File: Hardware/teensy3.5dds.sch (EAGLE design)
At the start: 105 parts, among them IC1 AD8034, IC2 AD8034, IC3 AD8034, IC4 AD8034, IC5 AD8034, IC6 AD737KRZ-R7, IC7 AD8034, IC8 AD8034, J1 1776275-2, J2 1776275-2, Q1 10MHz, U1 TEENSY_3.5/3.6_BASIC, U2 ATMEGA32U4-AU, X1 1-227161-0

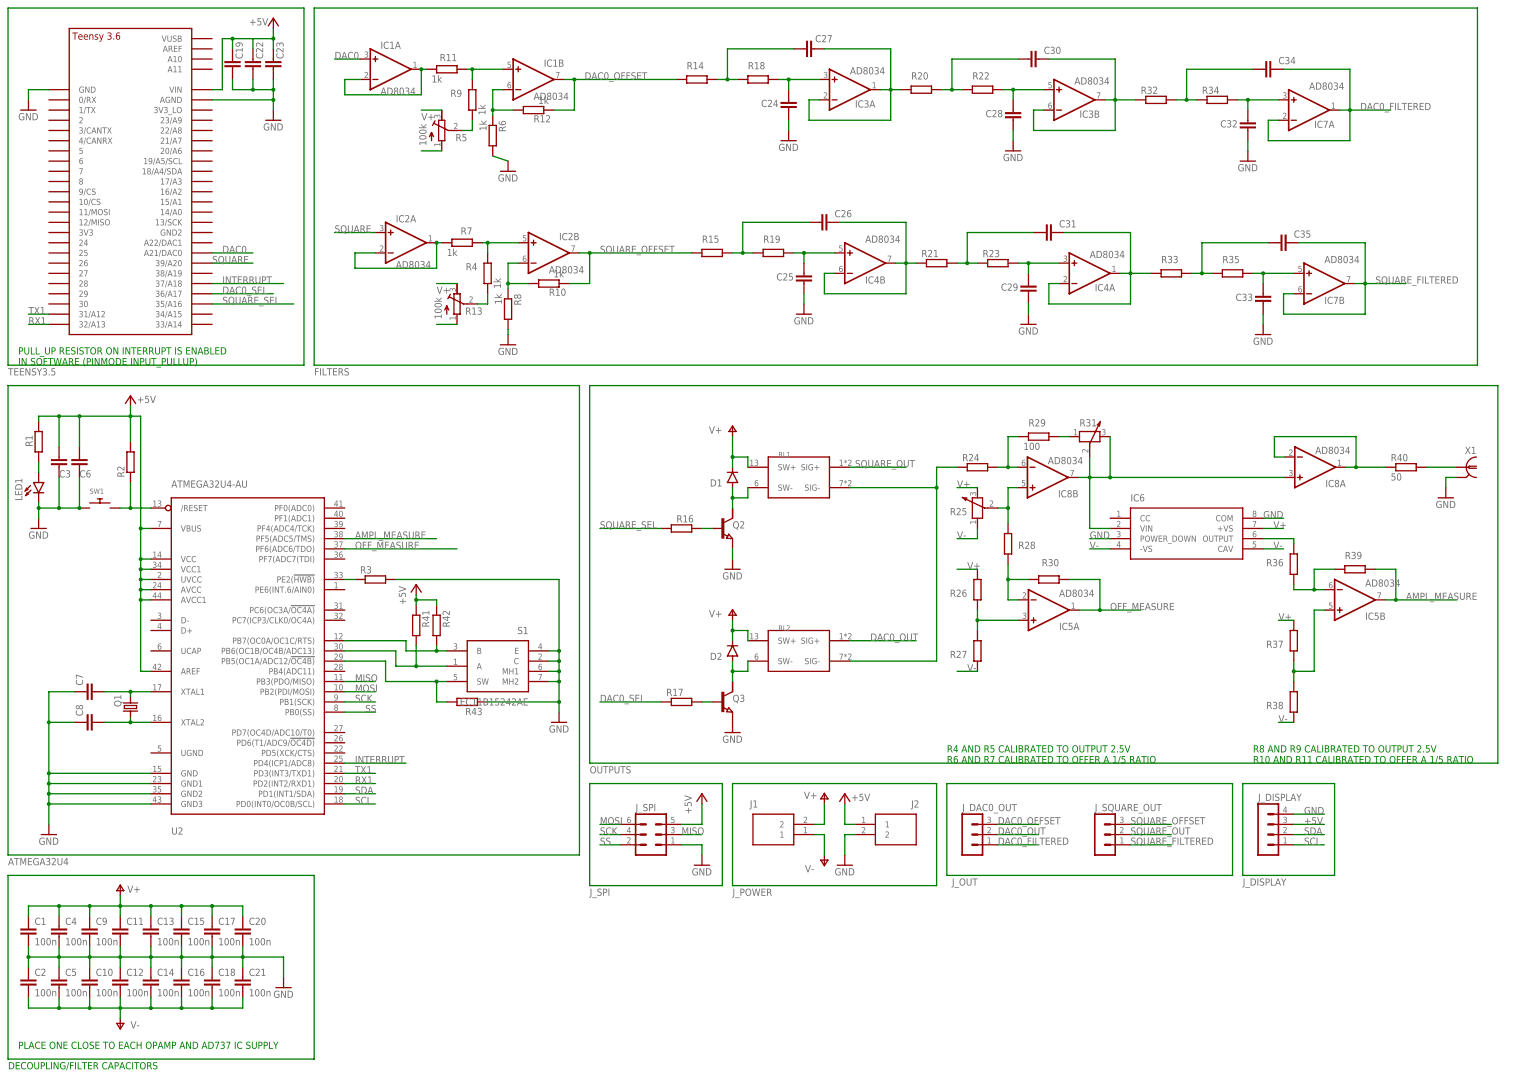
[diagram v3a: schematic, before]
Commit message: an actually working filter for the square wave
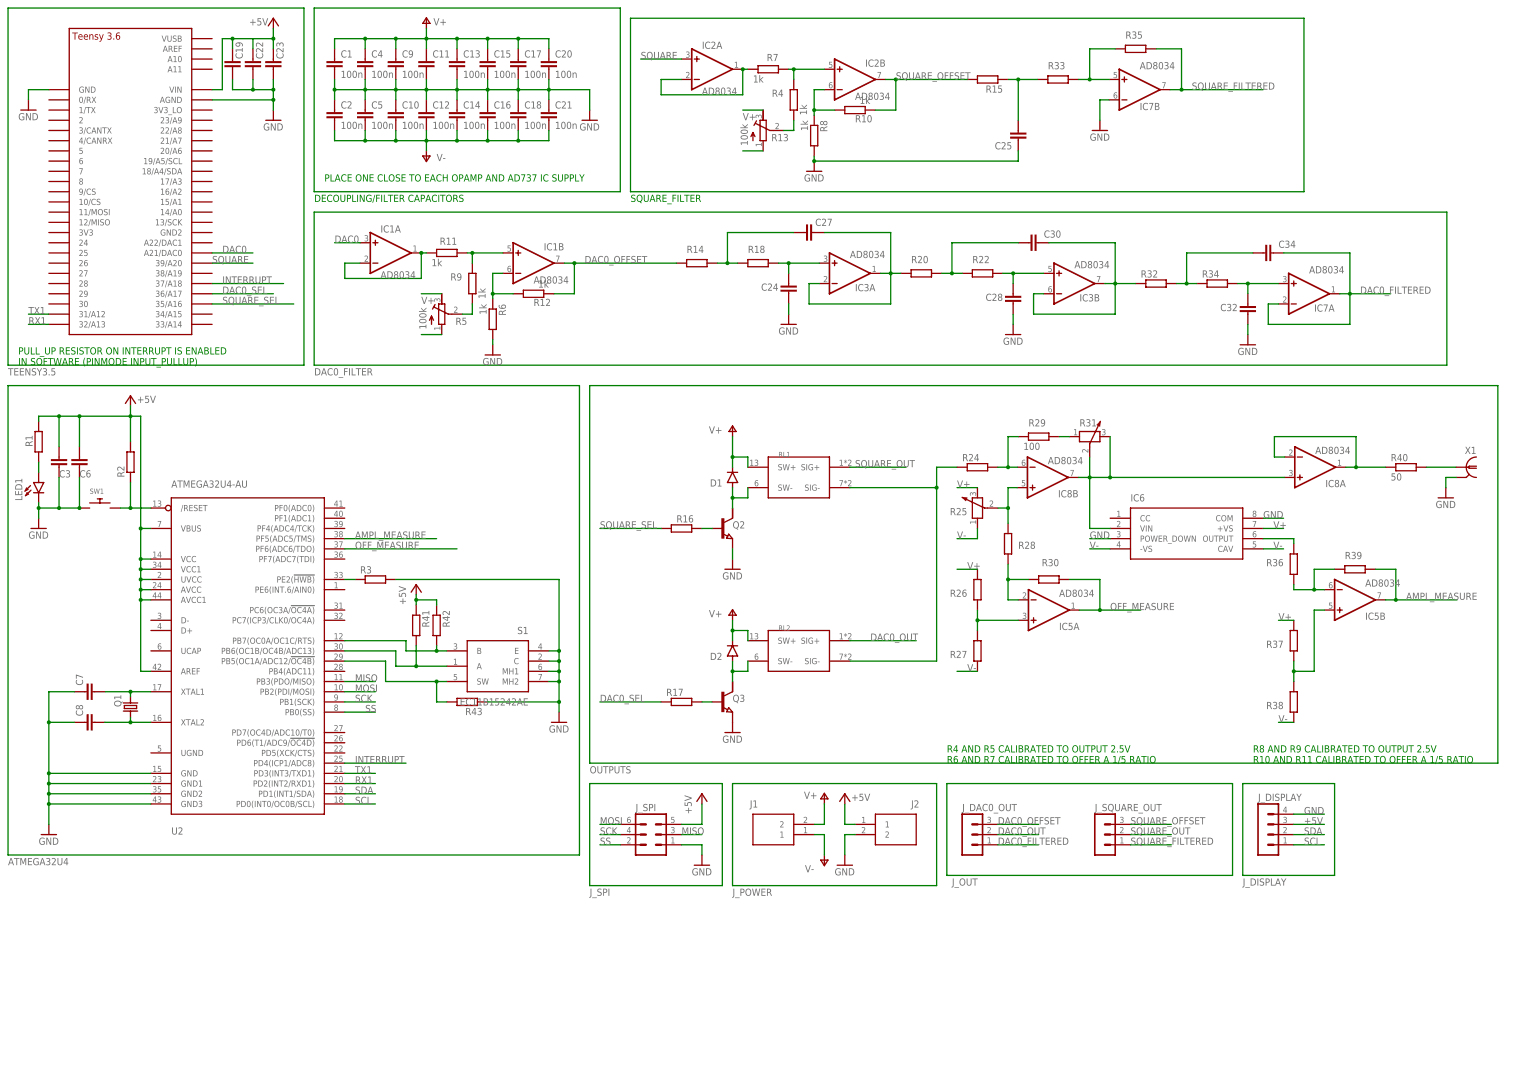
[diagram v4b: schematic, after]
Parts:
- removed C26, C31, C35: 100p, rcl:C-EUC0805
- removed C29, C33: 10p, rcl:C-EUC0805
- removed IC4: AD8034, linear:TL082D
- removed R19: 4.75k, rcl:R-EU_M0805
- removed R21: 150, rcl:R-EU_R0805
- removed R23: 3.74k, rcl:R-EU_R0805
- C25: value 10p -> (none)
- R15: value 130 -> (none); device rcl:R-EU_M0805 -> rcl:R-EU_R0805
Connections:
- removed net N$66: C31.2, R21.2, R23.1
- removed net N$67: C31.1, IC4A.-IN, IC4A.OUT, R33.1
- removed net N$68: C29.2, IC4A.+IN, R23.2
- removed net N$69: C26.1, R15.2, R19.1
- removed net N$70: C26.2, IC4B.-IN, IC4B.OUT, R21.1
- removed net N$71: C25.2, IC4B.+IN, R19.2
- removed net N$76: C35.1, R33.2, R35.1
- removed net N$78: C33.2, IC7B.+IN, R35.2
- new net N$1: IC7B.+IN, R33.2, R35.1
- new net N$34: C25.2, R15.1, R33.1
- net GND: now also IC7B.-IN; no longer C29.1, C33.1
- net SQUARE_FILTERED: now also R35.2; no longer C35.2, IC7B.-IN
- net SQUARE_OFFSET: now also R15.2; no longer R15.1
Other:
- note added: "SQUARE_FILTER"
- moved on the sheet: C1, C10, C11, C12, C13, C14, C15, C16, C17, C18, C2, C20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

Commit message: board redisegn
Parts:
- removed C11: (no value), rcl:C-EUC0805
- removed C12: 100n, rcl:C-EUC0805
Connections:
- net GND: no longer C11.2, C12.1
- net N$25: now also U2.PC7(ICP3/CLK0/OC4A); no longer U2.PB6(OC1B/OC4B/ADC13)
- net N$29: now also U2.PB6(OC1B/OC4B/ADC13); no longer U2.PB5(OC1A/ADC12/!OC4B)
- net N$8: now also U2.PC6(OC3A/!OC4A); no longer U2.PB7(OC0A/OC1C/RTS)
- net V+: no longer C11.1
- net V-: no longer C12.2
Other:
- moved on the sheet: C25
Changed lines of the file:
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@@
 <setting verticaltext="up"/>
 </settings>
-<grid distance="0.1" unitdist="inch" unit="inch" style="lines" multiple="1" display="yes" altdistance="0.05" altunitdist="inch" altunit="inch"/>
+<grid distance="0.1" unitdist="inch" unit="inch" style="lines" multiple="1" display="no" altdistance="0.01" altunitdist="inch" altunit="inch"/>
 <layers>
 <layer number="1" name="Top" color="4" fill="1" visible="no" active="no"/>
@@
 <part name="C4" library="rcl" library_urn="urn:adsk.eagle:library:334" deviceset="C-EU" device="C0805" package3d_urn="urn:adsk.eagle:package:23617/2" value="100n"/>
 <part name="C9" library="rcl" library_urn="urn:adsk.eagle:library:334" deviceset="C-EU" device="C0805" package3d_urn="urn:adsk.eagle:package:23617/2" value="100n"/>
-<part name="C11" library="rcl" library_urn="urn:adsk.eagle:library:334" deviceset="C-EU" device="C0805" package3d_urn="urn:adsk.eagle:package:23617/2"/>
 <part name="C13" library="rcl" library_urn="urn:adsk.eagle:library:334" deviceset="C-EU" device="C0805" package3d_urn="urn:adsk.eagle:package:23617/2" value="100n"/>
 <part name="C15" library="rcl" library_urn="urn:adsk.eagle:library:334" deviceset="C-EU" device="C0805" package3d_urn="urn:adsk.eagle:package:23617/2" value="100n"/>
@@
 <part name="C5" library="rcl" library_urn="urn:adsk.eagle:library:334" deviceset="C-EU" device="C0805" package3d_urn="urn:adsk.eagle:package:23617/2" value="100n"/>
 <part name="C10" library="rcl" library_urn="urn:adsk.eagle:library:334" deviceset="C-EU" device="C0805" package3d_urn="urn:adsk.eagle:package:23617/2" value="100n"/>
-<part name="C12" library="rcl" library_urn="urn:adsk.eagle:library:334" deviceset="C-EU" device="C0805" package3d_urn="urn:adsk.eagle:package:23617/2" value="100n"/>
 <part name="C14" library="rcl" library_urn="urn:adsk.eagle:library:334" deviceset="C-EU" device="C0805" package3d_urn="urn:adsk.eagle:package:23617/2" value="100n"/>
 <part name="C16" library="rcl" library_urn="urn:adsk.eagle:library:334" deviceset="C-EU" device="C0805" package3d_urn="urn:adsk.eagle:package:23617/2" value="100n"/>
@@
 <part name="R15" library="rcl" library_urn="urn:adsk.eagle:library:334" deviceset="R-EU_" device="R0805" package3d_urn="urn:adsk.eagle:package:23553/2"/>
 <part name="C25" library="rcl" library_urn="urn:adsk.eagle:library:334" deviceset="C-EU" device="C0805" package3d_urn="urn:adsk.eagle:package:23617/2"/>
+<part name="GND4" library="supply1" library_urn="urn:adsk.eagle:library:371" deviceset="GND" device=""/>
 </parts>
 <sheets>
@@
 <attribute name="VALUE" x="67.564" y="15.621" size="1.778" layer="96"/>
 </instance>
-<instance part="C11" gate="G$1" x="73.66" y="20.32" smashed="yes">
-<attribute name="NAME" x="75.184" y="20.701" size="1.778" layer="95"/>
-<attribute name="VALUE" x="75.184" y="15.621" size="1.778" layer="96"/>
-</instance>
 <instance part="C13" gate="G$1" x="81.28" y="20.32" smashed="yes">
 <attribute name="NAME" x="82.804" y="20.701" size="1.778" layer="95"/>
@@
 <attribute name="VALUE" x="67.564" y="2.921" size="1.778" layer="96"/>
 </instance>
-<instance part="C12" gate="G$1" x="73.66" y="7.62" smashed="yes">
-<attribute name="NAME" x="75.184" y="8.001" size="1.778" layer="95"/>
-<attribute name="VALUE" x="75.184" y="2.921" size="1.778" layer="96"/>
-</instance>
 <instance part="C14" gate="G$1" x="81.28" y="7.62" smashed="yes">
 <attribute name="NAME" x="82.804" y="8.001" size="1.778" layer="95"/>
@@
 <attribute name="VALUE" x="217.17" y="18.542" size="1.778" layer="96" rot="R180"/>
 </instance>
-<instance part="C25" gate="G$1" x="220.98" y="0" smashed="yes" rot="R180">
-<attribute name="NAME" x="219.456" y="-0.381" size="1.778" layer="95" rot="R180"/>
-<attribute name="VALUE" x="219.456" y="4.699" size="1.778" layer="96" rot="R180"/>
+<instance part="C25" gate="G$1" x="220.98" y="2.54" smashed="yes" rot="R180">
+<attribute name="NAME" x="219.456" y="2.159" size="1.778" layer="95" rot="R180"/>
+<attribute name="VALUE" x="219.456" y="7.239" size="1.778" layer="96" rot="R180"/>
+</instance>
+<instance part="GND4" gate="1" x="220.98" y="-7.62" smashed="yes">
+<attribute name="VALUE" x="218.44" y="-10.16" size="1.778" layer="96"/>
 </instance>
 </instances>
@@
 <pinref part="C13" gate="G$1" pin="2"/>
 <wire x1="81.28" y1="12.7" x2="81.28" y2="15.24" width="0.1524" layer="91"/>
-<pinref part="C11" gate="G$1" pin="2"/>
 <wire x1="73.66" y1="15.24" x2="73.66" y2="12.7" width="0.1524" layer="91"/>
 <junction x="73.66" y="12.7"/>
-<pinref part="C12" gate="G$1" pin="1"/>
 <wire x1="73.66" y1="10.16" x2="73.66" y2="12.7" width="0.1524" layer="91"/>
 <pinref part="C9" gate="G$1" pin="2"/>
@@
 </segment>
 <segment>
+<pinref part="R8" gate="G$1" pin="2"/>
 <pinref part="GND17" gate="1" pin="GND"/>
-<pinref part="R8" gate="G$1" pin="2"/>
 <wire x1="170.18" y1="-5.08" x2="170.18" y2="-3.81" width="0.1524" layer="91"/>
-<pinref part="C25" gate="G$1" pin="1"/>
-<wire x1="220.98" y1="-2.54" x2="220.98" y2="-5.08" width="0.1524" layer="91"/>
-<wire x1="220.98" y1="-5.08" x2="170.18" y2="-5.08" width="0.1524" layer="91"/>
-<junction x="170.18" y="-5.08"/>
 </segment>
 <segment>
@@
 <wire x1="241.3" y1="10.16" x2="241.3" y2="5.08" width="0.1524" layer="91"/>
 </segment>
+<segment>
+<pinref part="C25" gate="G$1" pin="1"/>
+<wire x1="220.98" y1="0" x2="220.98" y2="-5.08" width="0.1524" layer="91"/>
+<pinref part="GND4" gate="1" pin="GND"/>
+</segment>
 </net>
 <net name="DAC0" class="1">
@@
 <wire x1="66.04" y1="22.86" x2="66.04" y2="25.4" width="0.1524" layer="91"/>
 <junction x="66.04" y="25.4"/>
-<pinref part="C11" gate="G$1" pin="1"/>
 <wire x1="73.66" y1="22.86" x2="73.66" y2="25.4" width="0.1524" layer="91"/>
 <pinref part="C13" gate="G$1" pin="1"/>
@@
 <wire x1="66.04" y1="2.54" x2="66.04" y2="0" width="0.1524" layer="91"/>
 <junction x="66.04" y="0"/>
-<pinref part="C12" gate="G$1" pin="2"/>
 <wire x1="73.66" y1="2.54" x2="73.66" y2="0" width="0.1524" layer="91"/>
 <pinref part="C14" gate="G$1" pin="2"/>
@@
 <net name="N$8" class="0">
 <segment>
-<pinref part="U2" gate="G$1" pin="PB7(OC0A/OC1C/RTS)"/>
-<wire x1="53.34" y1="-124.46" x2="68.58" y2="-124.46" width="0.1524" layer="91"/>
-<wire x1="68.58" y1="-124.46" x2="68.58" y2="-127" width="0.1524" layer="91"/>
 <pinref part="S1" gate="G$1" pin="B"/>
 <wire x1="68.58" y1="-127" x2="76.2" y2="-127" width="0.1524" layer="91"/>
@@
 <wire x1="76.2" y1="-125.73" x2="76.2" y2="-127" width="0.1524" layer="91"/>
 <junction x="76.2" y="-127"/>
+<pinref part="U2" gate="G$1" pin="PC6(OC3A/!OC4A)"/>
+<wire x1="53.34" y1="-116.84" x2="68.58" y2="-116.84" width="0.1524" layer="91"/>
+<wire x1="68.58" y1="-116.84" x2="68.58" y2="-127" width="0.1524" layer="91"/>
 </segment>
 </net>
 <net name="N$25" class="0">
 <segment>
-<pinref part="U2" gate="G$1" pin="PB6(OC1B/OC4B/ADC13)"/>
-<wire x1="53.34" y1="-127" x2="66.04" y2="-127" width="0.1524" layer="91"/>
-<wire x1="66.04" y1="-127" x2="66.04" y2="-130.81" width="0.1524" layer="91"/>
 <pinref part="S1" gate="G$1" pin="A"/>
 <wire x1="66.04" y1="-130.81" x2="71.12" y2="-130.81" width="0.1524" layer="91"/>
@@
 <wire x1="71.12" y1="-125.73" x2="71.12" y2="-130.81" width="0.1524" layer="91"/>
 <junction x="71.12" y="-130.81"/>
+<pinref part="U2" gate="G$1" pin="PC7(ICP3/CLK0/OC4A)"/>
+<wire x1="53.34" y1="-119.38" x2="66.04" y2="-119.38" width="0.1524" layer="91"/>
+<wire x1="66.04" y1="-119.38" x2="66.04" y2="-130.81" width="0.1524" layer="91"/>
 </segment>
 </net>
@@
 <wire x1="78.74" y1="-134.62" x2="76.2" y2="-134.62" width="0.1524" layer="91"/>
 <wire x1="76.2" y1="-134.62" x2="63.5" y2="-134.62" width="0.1524" layer="91"/>
-<wire x1="63.5" y1="-134.62" x2="63.5" y2="-129.54" width="0.1524" layer="91"/>
-<pinref part="U2" gate="G$1" pin="PB5(OC1A/ADC12/!OC4B)"/>
-<wire x1="63.5" y1="-129.54" x2="53.34" y2="-129.54" width="0.1524" layer="91"/>
 <pinref part="R43" gate="G$1" pin="2"/>
 <wire x1="78.74" y1="-139.7" x2="76.2" y2="-139.7" width="0.1524" layer="91"/>
 <wire x1="76.2" y1="-139.7" x2="76.2" y2="-134.62" width="0.1524" layer="91"/>
 <junction x="76.2" y="-134.62"/>
+<wire x1="63.5" y1="-127" x2="63.5" y2="-134.62" width="0.1524" layer="91"/>
+<pinref part="U2" gate="G$1" pin="PB6(OC1B/OC4B/ADC13)"/>
+<wire x1="53.34" y1="-127" x2="63.5" y2="-127" width="0.1524" layer="91"/>
 </segment>
 </net>
@@
 <pinref part="C25" gate="G$1" pin="2"/>
 <pinref part="R15" gate="G$1" pin="1"/>
-<wire x1="220.98" y1="5.08" x2="220.98" y2="15.24" width="0.1524" layer="91"/>
+<wire x1="220.98" y1="7.62" x2="220.98" y2="15.24" width="0.1524" layer="91"/>
 <wire x1="220.98" y1="15.24" x2="218.44" y2="15.24" width="0.1524" layer="91"/>
 <pinref part="R33" gate="G$1" pin="1"/>
